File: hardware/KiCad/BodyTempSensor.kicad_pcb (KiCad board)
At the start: 4 copper layers, 80 x 35 mm, 79 parts, among them IC3 TMP117MAIDRVR, IC4 TMP117MAIDRVT, IC5 TMP117MAIDRVT, IC6 TMP117MAIDRVT, IC7 NRF54L15-QFAA-R, J1 USB_C_Receptacle_USB2.0, J3 BAT, J6 Conn_02x05_Odd_Even, U2 USBLC6-2SC6, U3 MCP73833-xxx-UN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

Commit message: Updated KiCad and BOM
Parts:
- removed C26: 100n, Capacitor_SMD:C_0402_1005Metric_Pad0.74x0.62mm_HandSolder
- added Q1: NMOS, Package_TO_SOT_SMD:SOT-23, F.Cu at (159.6, 121.0)
- added Q2: NMOS, Package_TO_SOT_SMD:SOT-23, F.Cu at (180.4, 124.4)
- C1, C10, C11, C3, C5, C7: moved to F.Cu
- C2: footprint Capacitor_SMD:C_0504_1310Metric_Pad0.83x1.28mm_HandSolder -> Capacitor_SMD:C_0402_1005Metric_Pad0.74x0.62mm_HandSolder
- D1, D2, D3: footprint LED_SMD:LED_0603_1608Metric_Pad1.05x0.95mm_HandSolder -> LED_SMD:LED_0402_1005Metric_Pad0.77x0.64mm_HandSolder
- H1, H2: value MountingHole_Pad -> ~
- IC3: value TMP117MAIDRVR -> TMP117MAIDRVT; footprint LibLoader:SON65P200X200X80-7N -> PCB_Lib_ItsNotDaan:SON65P200X200X80-7N
- IC4, IC5, IC6: footprint LibLoader:SON65P200X200X80-7N -> PCB_Lib_ItsNotDaan:SON65P200X200X80-7N
- IC7: footprint LibLoader:QFN40P600X600X95-49N -> PCB_Lib_ItsNotDaan:QFN40P600X600X95-49N
- J1: footprint Connector_USB:USB_C_Receptacle_GCT_USB4105-xx-A_16P_TopMnt_Horizontal -> PCB_Lib_ItsNotDaan:USB_C_Receptacle_GCT_USB4105-xx-A_16P_TopMnt_Horizontal
- L1, L4: value 3.5nH -> 3n5; footprint Inductor_SMD:L_0201_0603Metric -> Inductor_SMD:L_0201_0603Metric_Pad0.64x0.40mm_HandSolder
- L3: value 2.7nH -> 2n7; footprint Inductor_SMD:L_0201_0603Metric -> Inductor_SMD:L_0402_1005Metric_Pad0.77x0.64mm_HandSolder
- L5: footprint Inductor_SMD:L_0201_0603Metric -> Inductor_SMD:L_0603_1608Metric_Pad1.05x0.95mm_HandSolder
- moved TP1 56.3 mm to (132.0, 123.0)
- moved H1 49.1 mm to (225.8, 132.6)
- moved H2 49.1 mm to (215.8, 132.6)
- moved C18 36.3 mm to (216.1, 117.9)
- moved R11 36.3 mm to (222.9, 118.8)
- moved R13 36.3 mm to (220.4, 122.3)
- moved R14 36.3 mm to (220.4, 121.2)
- moved R17 36.3 mm to (216.1, 119.0)
- moved U5 36.3 mm to (216.8, 121.3)
- moved R25 28.4 mm to (177.7, 126.0), turned to 90 degrees
- moved R28 27.8 mm to (180.1, 126.8)
- moved C12 25.7 mm to (202.6, 130.4)
- moved LED1 25.7 mm to (205.2, 130.4)
- moved TP2 25.7 mm to (205.8, 129.4)
- moved C3 16.8 mm to (177.8, 94.2), turned to 90 degrees
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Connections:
- C11 pad 1: VBUS -> +3V3
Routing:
- net Net-(IC7A-DECD): track 0.00 -> 6.06 mm
- net Earth: track 2.27 -> 8.00 mm
- net /RF: track 0.00 -> 4.97 mm
- net /OSC_OUT: track 6.17 -> 10.1 mm
- net VBUS: track 7.64 -> 3.86 mm, vias 1 -> 0
- net Net-(IC7A-DECRF): track 0.00 -> 3.69 mm
- net /OSC_IN: track 3.04 -> 6.25 mm
- net Net-(Q2-G): track 0.00 -> 3.20 mm
- net Net-(IC7A-DCC): track 0.00 -> 2.28 mm
- net /RF2: track 0.00 -> 2.23 mm
- net Net-(C8-Pad1): track 0.00 -> 1.31 mm
- net +3V3: vias 5 -> 0

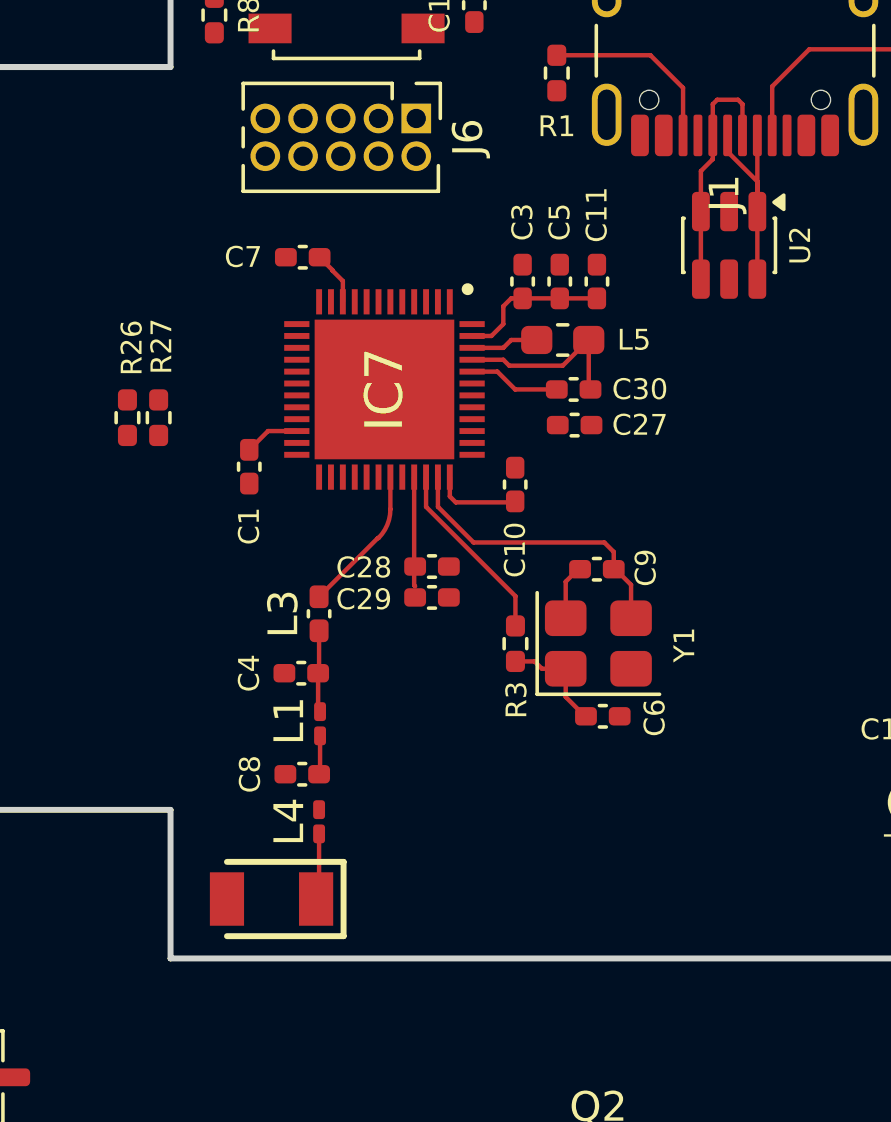
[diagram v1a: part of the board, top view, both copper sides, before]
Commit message: Small edit on the PCB ANT
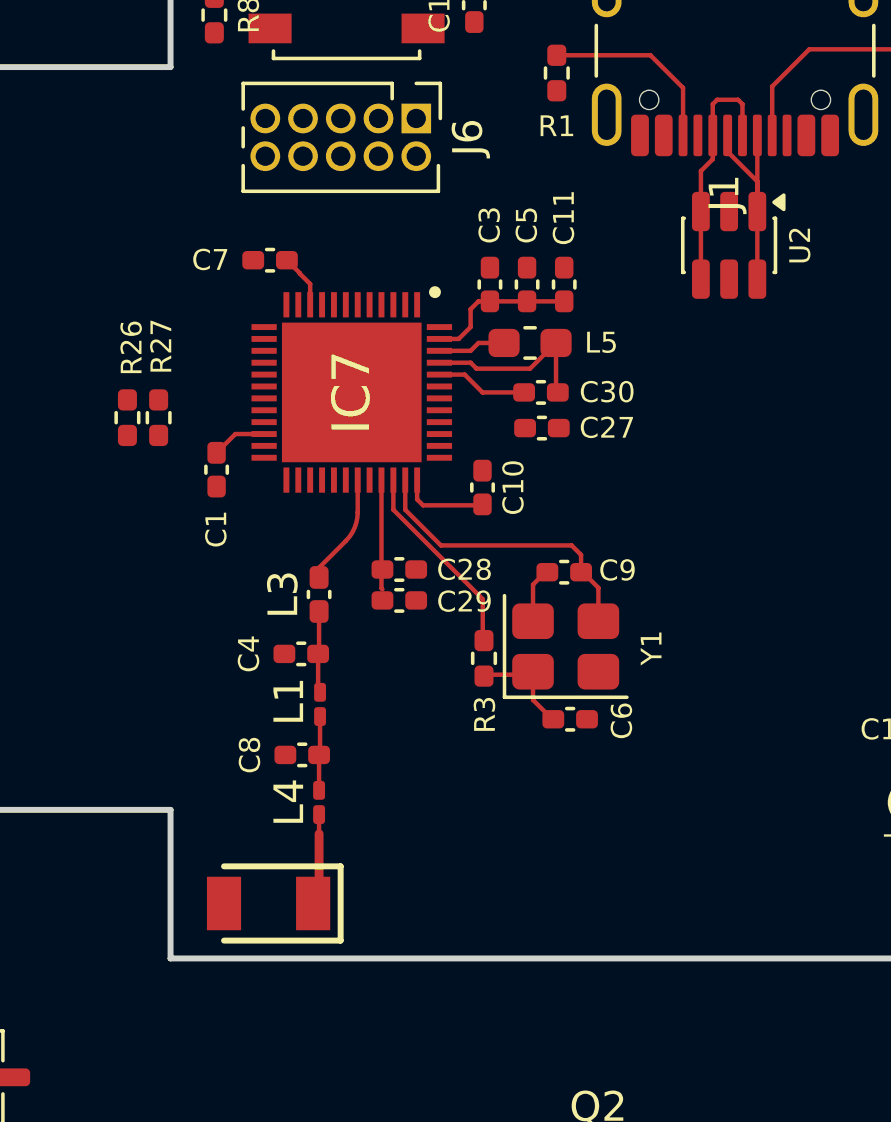
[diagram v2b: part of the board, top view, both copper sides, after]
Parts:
- moved R3 1.17 mm to (176.6, 106.9)
- moved C29 1.10 mm to (173.7, 105.0)
- moved C6 1.10 mm to (179.4, 109.0)
- moved C28 1.10 mm to (173.7, 103.9)
- moved C10 1.10 mm to (176.5, 101.2)
- moved C27 1.10 mm to (178.5, 99.2)
- moved C30 1.10 mm to (178.5, 98.0)
- moved IC7 1.10 mm to (172.1, 98.0)
- moved C1 1.10 mm to (167.6, 100.5)
- moved C11 1.10 mm to (179.2, 94.3)
- moved C3 1.10 mm to (176.8, 94.3)
- moved C5 1.10 mm to (178.0, 94.3)
- moved C7 1.10 mm to (169.3, 93.5)
- moved C9 1.10 mm to (179.2, 104.0)
- moved L5 1.10 mm to (178.1, 96.3)
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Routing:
- net /RF: track 4.97 -> 3.75 mm
- net Net-(C8-Pad1): track 1.31 -> 2.50 mm
- net /RF2: track 2.23 -> 2.88 mm
